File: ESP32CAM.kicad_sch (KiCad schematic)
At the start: 14 parts, among them J10 Conn_01x02, J12 USB_C_Receptacle_USB2.0, U12 ESP32-CAM, U9 FT231XQ

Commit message: Rev 2 PCB
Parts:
- U12: now not fitted
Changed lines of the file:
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@@
 		(in_bom yes)
 		(on_board yes)
-		(dnp no)
+		(dnp yes)
 		(fields_autoplaced yes)
 		(property "Reference" "U12"

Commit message: Rev 2 finished
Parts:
- C28: LCSC Part # C1525 -> C307331
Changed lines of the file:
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@@
 			)
 		)
-		(property "LCSC Part #" "C1525"
+		(property "LCSC Part #" "C307331"
 			(at 129.54 58.293 0)
 			(effects

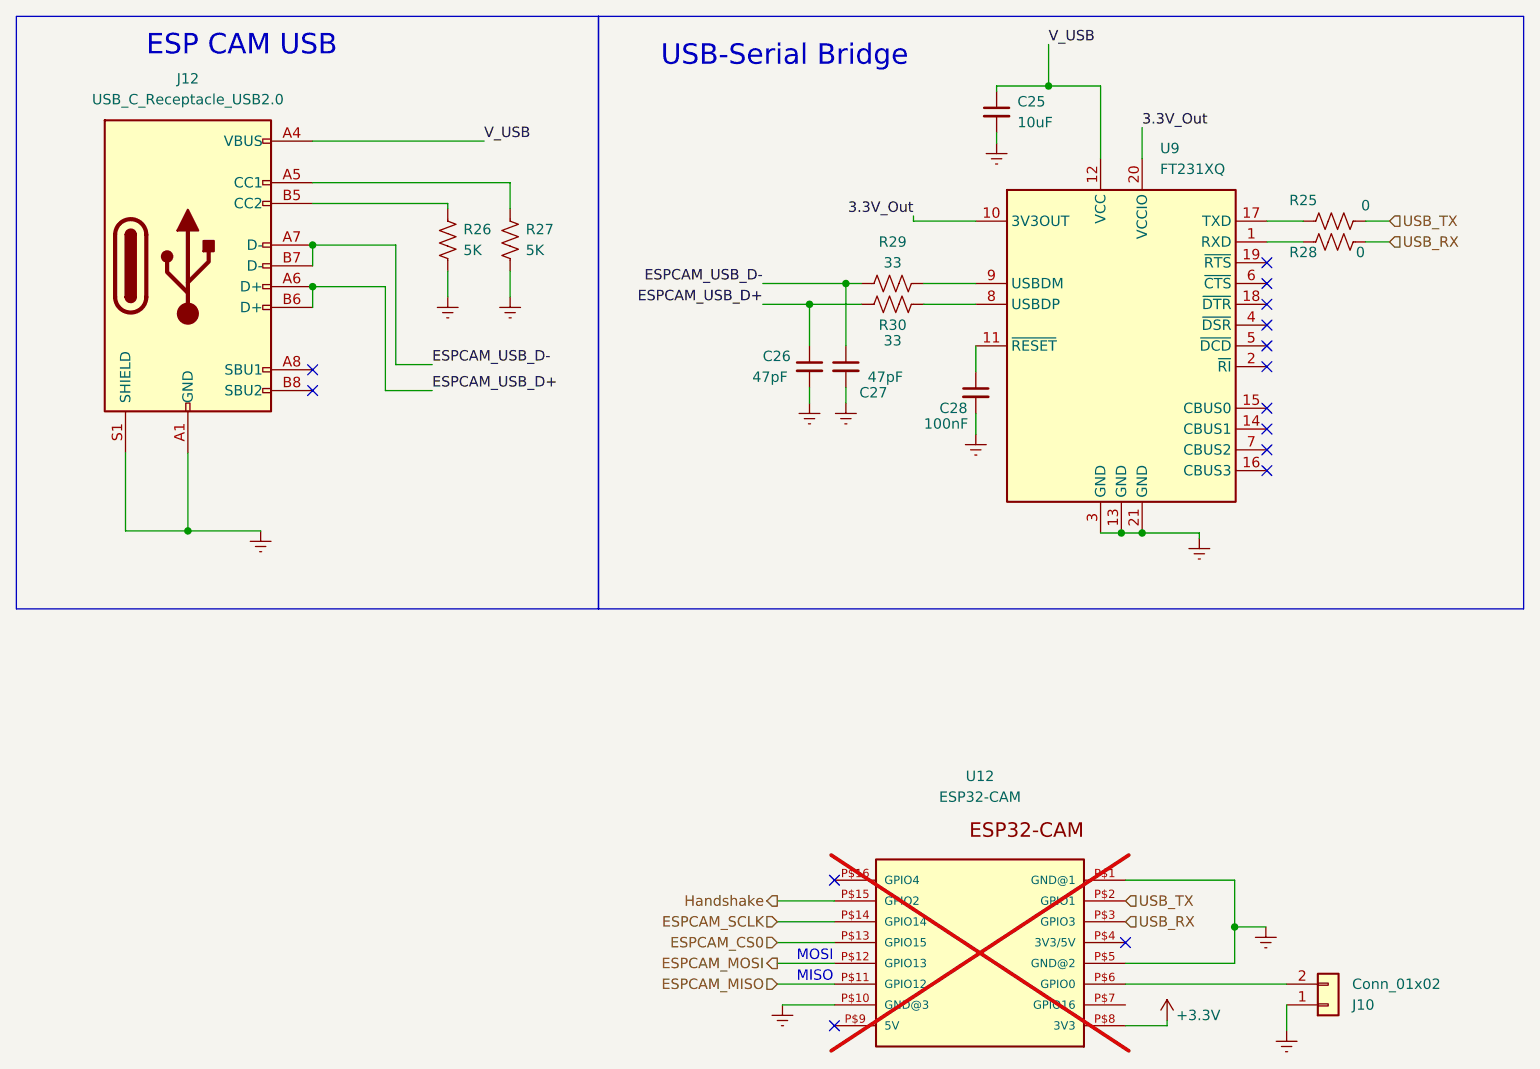
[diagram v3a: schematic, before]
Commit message: Fixed reference errors and bootstrap pin assignments
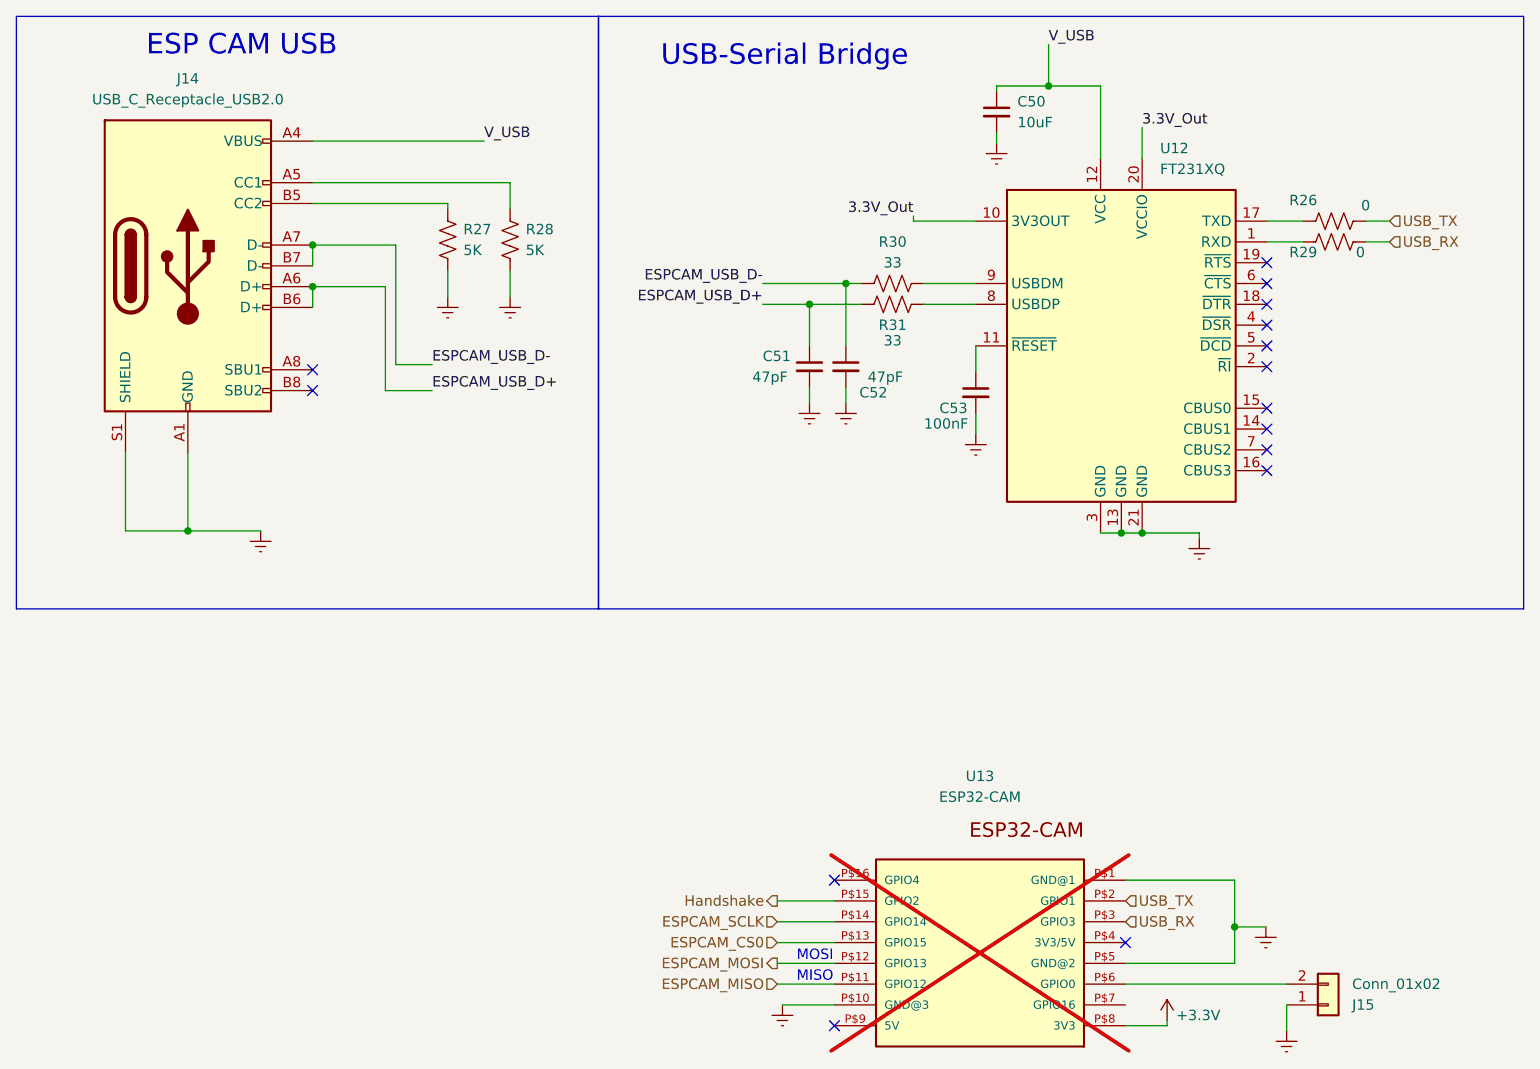
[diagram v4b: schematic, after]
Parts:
- renumbered C25 to C50, C26 to C51, C27 to C52, C28 to C53, J12 to J14, J10 to J15, R25 to R26, R26 to R27, R27 to R28, R28 to R29, R29 to R30, R30 to R31, U9 to U12, U12 to U13
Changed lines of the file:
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@@
 		(on_board no)
 		(dnp no)
-		(property "Reference" "#PWR0105"
+		(property "Reference" "#PWR0125"
 			(at 152.908 138.811 0)
 			(effects
@@
 			(project "DeltaRhoRobot"
 				(path "/cced1a6d-3dc4-42b2-93bd-998a7b4cf4e8/5eb80655-957d-4a1c-8d7d-b2e173715026/ba807c80-2a51-4f5f-8aa4-02e2ddffef6a"
-					(reference "#PWR0105")
+					(reference "#PWR0125")
 					(unit 1)
 				)
@@
 		(dnp no)
 		(fields_autoplaced yes)
-		(property "Reference" "#PWR098"
+		(property "Reference" "#PWR0119"
 			(at 113.665 65.913 0)
 			(effects
@@
 			(project "DeltaRhoRobot"
 				(path "/cced1a6d-3dc4-42b2-93bd-998a7b4cf4e8/5eb80655-957d-4a1c-8d7d-b2e173715026/ba807c80-2a51-4f5f-8aa4-02e2ddffef6a"
-					(reference "#PWR098")
+					(reference "#PWR0119")
 					(unit 1)
 				)
@@
 		(dnp no)
 		(fields_autoplaced yes)
-		(property "Reference" "#PWR0104"
+		(property "Reference" "#PWR0126"
 			(at 167.513 142.621 0)
 			(effects
@@
 			(project "DeltaRhoRobot"
 				(path "/cced1a6d-3dc4-42b2-93bd-998a7b4cf4e8/5eb80655-957d-4a1c-8d7d-b2e173715026/ba807c80-2a51-4f5f-8aa4-02e2ddffef6a"
-					(reference "#PWR0104")
+					(reference "#PWR0126")
 					(unit 1)
 				)
@@
 		(dnp no)
 		(fields_autoplaced yes)
-		(property "Reference" "J12"
+		(property "Reference" "J14"
 			(at 33.274 19.939 0)
 			(effects
@@
 			(project "DeltaRhoRobot"
 				(path "/cced1a6d-3dc4-42b2-93bd-998a7b4cf4e8/5eb80655-957d-4a1c-8d7d-b2e173715026/ba807c80-2a51-4f5f-8aa4-02e2ddffef6a"
-					(reference "J12")
+					(reference "J14")
 					(unit 1)
 				)
@@
 		(dnp no)
 		(fields_autoplaced yes)
-		(property "Reference" "#PWR0102"
+		(property "Reference" "#PWR0123"
 			(at 164.973 129.921 0)
 			(effects
@@
 			(project "DeltaRhoRobot"
 				(path "/cced1a6d-3dc4-42b2-93bd-998a7b4cf4e8/5eb80655-957d-4a1c-8d7d-b2e173715026/ba807c80-2a51-4f5f-8aa4-02e2ddffef6a"
-					(reference "#PWR0102")
+					(reference "#PWR0123")
 					(unit 1)
 				)
@@
 		(dnp no)
 		(fields_autoplaced yes)
-		(property "Reference" "U9"
+		(property "Reference" "U12"
 			(at 152.0541 28.448 0)
 			(effects
@@
 			(project "DeltaRhoRobot"
 				(path "/cced1a6d-3dc4-42b2-93bd-998a7b4cf4e8/5eb80655-957d-4a1c-8d7d-b2e173715026/ba807c80-2a51-4f5f-8aa4-02e2ddffef6a"
-					(reference "U9")
+					(reference "U12")
 					(unit 1)
 				)
@@
 		(on_board no)
 		(dnp no)
-		(property "Reference" "C28"
+		(property "Reference" "C53"
 			(at 125.095 60.198 0)
 			(effects
@@
 			(project "DeltaRhoRobot"
 				(path "/cced1a6d-3dc4-42b2-93bd-998a7b4cf4e8/5eb80655-957d-4a1c-8d7d-b2e173715026/ba807c80-2a51-4f5f-8aa4-02e2ddffef6a"
-					(reference "C28")
+					(reference "C53")
 					(unit 1)
 				)
@@
 		(on_board no)
 		(dnp no)
-		(property "Reference" "C27"
+		(property "Reference" "C52"
 			(at 118.745 58.293 0)
 			(effects
@@
 			(project "DeltaRhoRobot"
 				(path "/cced1a6d-3dc4-42b2-93bd-998a7b4cf4e8/5eb80655-957d-4a1c-8d7d-b2e173715026/ba807c80-2a51-4f5f-8aa4-02e2ddffef6a"
-					(reference "C27")
+					(reference "C52")
 					(unit 1)
 				)
@@
 		(dnp no)
 		(fields_autoplaced yes)
-		(property "Reference" "#PWR099"
+		(property "Reference" "#PWR0120"
 			(at 129.54 69.723 0)
 			(effects
@@
 			(project "DeltaRhoRobot"
 				(path "/cced1a6d-3dc4-42b2-93bd-998a7b4cf4e8/5eb80655-957d-4a1c-8d7d-b2e173715026/ba807c80-2a51-4f5f-8aa4-02e2ddffef6a"
-					(reference "#PWR099")
+					(reference "#PWR0120")
 					(unit 1)
 				)
@@
 		(dnp no)
 		(fields_autoplaced yes)
-		(property "Reference" "#PWR0101"
+		(property "Reference" "#PWR0122"
 			(at 156.845 82.423 0)
 			(effects
@@
 			(project "DeltaRhoRobot"
 				(path "/cced1a6d-3dc4-42b2-93bd-998a7b4cf4e8/5eb80655-957d-4a1c-8d7d-b2e173715026/ba807c80-2a51-4f5f-8aa4-02e2ddffef6a"
-					(reference "#PWR0101")
+					(reference "#PWR0122")
 					(unit 1)
 				)
@@
 		(dnp no)
 		(fields_autoplaced yes)
-		(property "Reference" "C25"
+		(property "Reference" "C50"
 			(at 134.62 22.7393 0)
 			(effects
@@
 			(project "DeltaRhoRobot"
 				(path "/cced1a6d-3dc4-42b2-93bd-998a7b4cf4e8/5eb80655-957d-4a1c-8d7d-b2e173715026/ba807c80-2a51-4f5f-8aa4-02e2ddffef6a"
-					(reference "C25")
+					(reference "C50")
 					(unit 1)
 				)
@@
 		(dnp no)
 		(fields_autoplaced yes)
-		(property "Reference" "#PWR097"
+		(property "Reference" "#PWR0118"
 			(at 109.22 65.913 0)
 			(effects
@@
 			(project "DeltaRhoRobot"
 				(path "/cced1a6d-3dc4-42b2-93bd-998a7b4cf4e8/5eb80655-957d-4a1c-8d7d-b2e173715026/ba807c80-2a51-4f5f-8aa4-02e2ddffef6a"
-					(reference "#PWR097")
+					(reference "#PWR0118")
 					(unit 1)
 				)
@@
 		(dnp no)
 		(fields_autoplaced yes)
-		(property "Reference" "#PWR095"
+		(property "Reference" "#PWR0116"
 			(at 65.024 52.959 0)
 			(effects
@@
 			(project "DeltaRhoRobot"
 				(path "/cced1a6d-3dc4-42b2-93bd-998a7b4cf4e8/5eb80655-957d-4a1c-8d7d-b2e173715026/ba807c80-2a51-4f5f-8aa4-02e2ddffef6a"
-					(reference "#PWR095")
+					(reference "#PWR0116")
 					(unit 1)
 				)
@@
 		(on_board no)
 		(dnp no)
-		(property "Reference" "R29"
+		(property "Reference" "R30"
 			(at 119.38 39.878 90)
 			(effects
@@
 			(project "DeltaRhoRobot"
 				(path "/cced1a6d-3dc4-42b2-93bd-998a7b4cf4e8/5eb80655-957d-4a1c-8d7d-b2e173715026/ba807c80-2a51-4f5f-8aa4-02e2ddffef6a"
-					(reference "R29")
+					(reference "R30")
 					(unit 1)
 				)
@@
 		(on_board no)
 		(dnp no)
-		(property "Reference" "J10"
+		(property "Reference" "J15"
 			(at 175.514 133.096 0)
 			(effects
@@
 			(project "DeltaRhoRobot"
 				(path "/cced1a6d-3dc4-42b2-93bd-998a7b4cf4e8/5eb80655-957d-4a1c-8d7d-b2e173715026/ba807c80-2a51-4f5f-8aa4-02e2ddffef6a"
-					(reference "J10")
+					(reference "J15")
 					(unit 1)
 				)
@@
 		(dnp yes)
 		(fields_autoplaced yes)
-		(property "Reference" "U12"
+		(property "Reference" "U13"
 			(at 130.048 105.156 0)
 			(effects
@@
 			(project "DeltaRhoRobot"
 				(path "/cced1a6d-3dc4-42b2-93bd-998a7b4cf4e8/5eb80655-957d-4a1c-8d7d-b2e173715026/ba807c80-2a51-4f5f-8aa4-02e2ddffef6a"
-					(reference "U12")
+					(reference "U13")
 					(unit 1)
 				)
@@
 		(dnp no)
 		(fields_autoplaced yes)
-		(property "Reference" "R27"
+		(property "Reference" "R28"
 			(at 74.549 38.354 0)
 			(effects
@@
 			(project "DeltaRhoRobot"
 				(path "/cced1a6d-3dc4-42b2-93bd-998a7b4cf4e8/5eb80655-957d-4a1c-8d7d-b2e173715026/ba807c80-2a51-4f5f-8aa4-02e2ddffef6a"
-					(reference "R27")
+					(reference "R28")
 					(unit 1)
 				)
@@
 		(on_board no)
 		(dnp no)
-		(property "Reference" "C26"
+		(property "Reference" "C51"
 			(at 103.505 53.848 0)
 			(effects
@@
 			(project "DeltaRhoRobot"
 				(path "/cced1a6d-3dc4-42b2-93bd-998a7b4cf4e8/5eb80655-957d-4a1c-8d7d-b2e173715026/ba807c80-2a51-4f5f-8aa4-02e2ddffef6a"
-					(reference "C26")
+					(reference "C51")
 					(unit 1)
 				)
@@
 		(dnp no)
 		(fields_autoplaced yes)
-		(property "Reference" "#PWR094"
+		(property "Reference" "#PWR0115"
 			(at 132.08 34.163 0)
 			(effects
@@
 			(project "DeltaRhoRobot"
 				(path "/cced1a6d-3dc4-42b2-93bd-998a7b4cf4e8/5eb80655-957d-4a1c-8d7d-b2e173715026/ba807c80-2a51-4f5f-8aa4-02e2ddffef6a"
-					(reference "#PWR094")
+					(reference "#PWR0115")
 					(unit 1)
 				)
@@
 		(on_board no)
 		(dnp no)
-		(property "Reference" "R30"
+		(property "Reference" "R31"
 			(at 119.38 50.038 90)
 			(effects
@@
 			(project "DeltaRhoRobot"
 				(path "/cced1a6d-3dc4-42b2-93bd-998a7b4cf4e8/5eb80655-957d-4a1c-8d7d-b2e173715026/ba807c80-2a51-4f5f-8aa4-02e2ddffef6a"
-					(reference "R30")
+					(reference "R31")
 					(unit 1)
 				)
@@
 		(dnp no)
 		(fields_autoplaced yes)
-		(property "Reference" "#PWR0100"
+		(property "Reference" "#PWR0121"
 			(at 42.164 81.534 0)
 			(effects
@@
 			(project "DeltaRhoRobot"
 				(path "/cced1a6d-3dc4-42b2-93bd-998a7b4cf4e8/5eb80655-957d-4a1c-8d7d-b2e173715026/ba807c80-2a51-4f5f-8aa4-02e2ddffef6a"
-					(reference "#PWR0100")
+					(reference "#PWR0121")
 					(unit 1)
 				)
@@
 		(on_board no)
 		(dnp no)
-		(property "Reference" "R28"
+		(property "Reference" "R29"
 			(at 169.545 41.148 90)
 			(effects
@@
 			(project "DeltaRhoRobot"
 				(path "/cced1a6d-3dc4-42b2-93bd-998a7b4cf4e8/5eb80655-957d-4a1c-8d7d-b2e173715026/ba807c80-2a51-4f5f-8aa4-02e2ddffef6a"
-					(reference "R28")
+					(reference "R29")
 					(unit 1)
 				)
@@
 		(dnp no)
 		(fields_autoplaced yes)
-		(property "Reference" "R26"
+		(property "Reference" "R27"
 			(at 66.929 38.354 0)
 			(effects
@@
 			(project "DeltaRhoRobot"
 				(path "/cced1a6d-3dc4-42b2-93bd-998a7b4cf4e8/5eb80655-957d-4a1c-8d7d-b2e173715026/ba807c80-2a51-4f5f-8aa4-02e2ddffef6a"
-					(reference "R26")
+					(reference "R27")
 					(unit 1)
 				)
@@
 		(dnp no)
 		(fields_autoplaced yes)
-		(property "Reference" "#PWR096"
+		(property "Reference" "#PWR0117"
 			(at 72.644 52.959 0)
 			(effects
@@
 			(project "DeltaRhoRobot"
 				(path "/cced1a6d-3dc4-42b2-93bd-998a7b4cf4e8/5eb80655-957d-4a1c-8d7d-b2e173715026/ba807c80-2a51-4f5f-8aa4-02e2ddffef6a"
-					(reference "#PWR096")
+					(reference "#PWR0117")
 					(unit 1)
 				)
@@
 		(dnp no)
 		(fields_autoplaced yes)
-		(property "Reference" "#PWR0103"
+		(property "Reference" "#PWR0124"
 			(at 105.918 139.446 0)
 			(effects
@@
 			(project "DeltaRhoRobot"
 				(path "/cced1a6d-3dc4-42b2-93bd-998a7b4cf4e8/5eb80655-957d-4a1c-8d7d-b2e173715026/ba807c80-2a51-4f5f-8aa4-02e2ddffef6a"
-					(reference "#PWR0103")
+					(reference "#PWR0124")
 					(unit 1)
 				)
@@
 		(on_board no)
 		(dnp no)
-		(property "Reference" "R25"
+		(property "Reference" "R26"
 			(at 169.545 34.798 90)
 			(effects
@@
 			(project "DeltaRhoRobot"
 				(path "/cced1a6d-3dc4-42b2-93bd-998a7b4cf4e8/5eb80655-957d-4a1c-8d7d-b2e173715026/ba807c80-2a51-4f5f-8aa4-02e2ddffef6a"
-					(reference "R25")
-					(unit 1)
-				)
+					(reference "R26")
+					(unit 1)
+				)
